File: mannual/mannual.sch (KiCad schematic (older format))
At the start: 31 parts, among them J1 Conn_02x07_Odd_Even, J10 Conn_02x10_Odd_Even, J2 Conn_01x02, J3 Conn_01x02, J4 Conn_01x02, J5 Conn_01x02, J6 Conn_01x02, J7 Conn_01x02, J8 Conn_01x02, J9 Conn_02x10_Odd_Even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

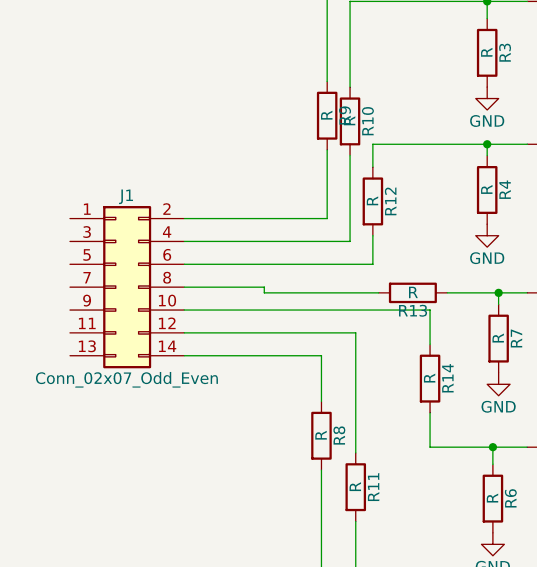
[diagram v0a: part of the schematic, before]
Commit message: Buck circuit also modified and pdfs also changed
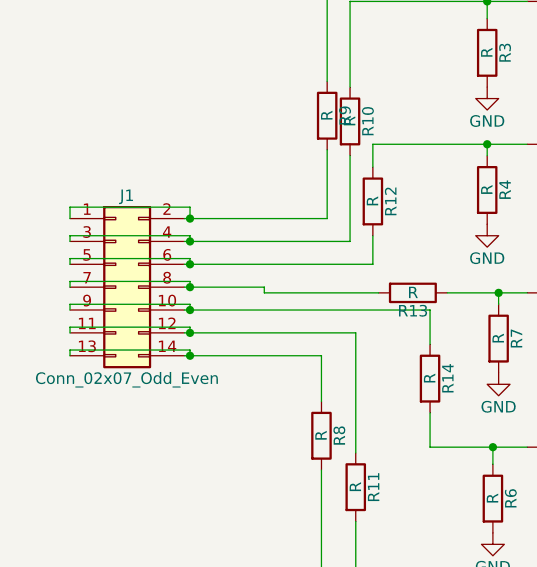
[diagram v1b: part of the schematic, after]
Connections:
- net at J1.1 (Pin_1): now also J1.2 (Pin_2), R9.2
- net at J1.10 (Pin_10), R14.1: now also J1.9 (Pin_9)
- net at J1.11 (Pin_11): now also J1.12 (Pin_12), R11.1
- net at J1.13 (Pin_13): now also J1.14 (Pin_14), R8.1
- net at J1.3 (Pin_3): now also J1.4 (Pin_4), R10.2
- net at J1.5 (Pin_5): now also J1.6 (Pin_6), R12.2
- net at J1.7 (Pin_7): now also J1.8 (Pin_8), R13.2
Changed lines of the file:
@@
 Wire Wire Line
 	6550 3125 7050 3125
+Wire Wire Line
+	1550 3325 1550 3300
+Wire Wire Line
+	1550 3300 2075 3300
+Wire Wire Line
+	2075 3300 2075 3325
+Connection ~ 2075 3325
+Wire Wire Line
+	1550 3425 1550 3400
+Wire Wire Line
+	1550 3400 2075 3400
+Wire Wire Line
+	2075 3400 2075 3425
+Connection ~ 2075 3425
+Wire Wire Line
+	1550 3525 1550 3500
+Wire Wire Line
+	1550 3500 2075 3500
+Wire Wire Line
+	2075 3500 2075 3525
+Connection ~ 2075 3525
+Wire Wire Line
+	1550 3625 1550 3600
+Wire Wire Line
+	1550 3600 2075 3600
+Wire Wire Line
+	2075 3600 2075 3625
+Connection ~ 2075 3625
+Wire Wire Line
+	1550 3725 1550 3700
+Wire Wire Line
+	1550 3700 2075 3700
+Wire Wire Line
+	2075 3700 2075 3725
+Connection ~ 2075 3725
+Wire Wire Line
+	1550 3825 1550 3800
+Wire Wire Line
+	1550 3800 2075 3800
+Wire Wire Line
+	2075 3800 2075 3825
+Connection ~ 2075 3825
+Wire Wire Line
+	1550 3225 1550 3175
+Wire Wire Line
+	1550 3175 2075 3175
+Wire Wire Line
+	2075 3175 2075 3225
+Connection ~ 2075 3225
 $EndSCHEMATC
